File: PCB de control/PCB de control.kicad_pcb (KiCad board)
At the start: 4 copper layers, 68.3 x 60 mm, 83 parts, among them J1 Conn_01x12_Pin, Q1 DMP4015SPSQ-13, U1 ESP32-C6-MINI-1U-H4, U2 DRV8434PWPR, U3 TPS54302DDCT, U4 TPS62162DSG, U5 D3V3XA4B10LP

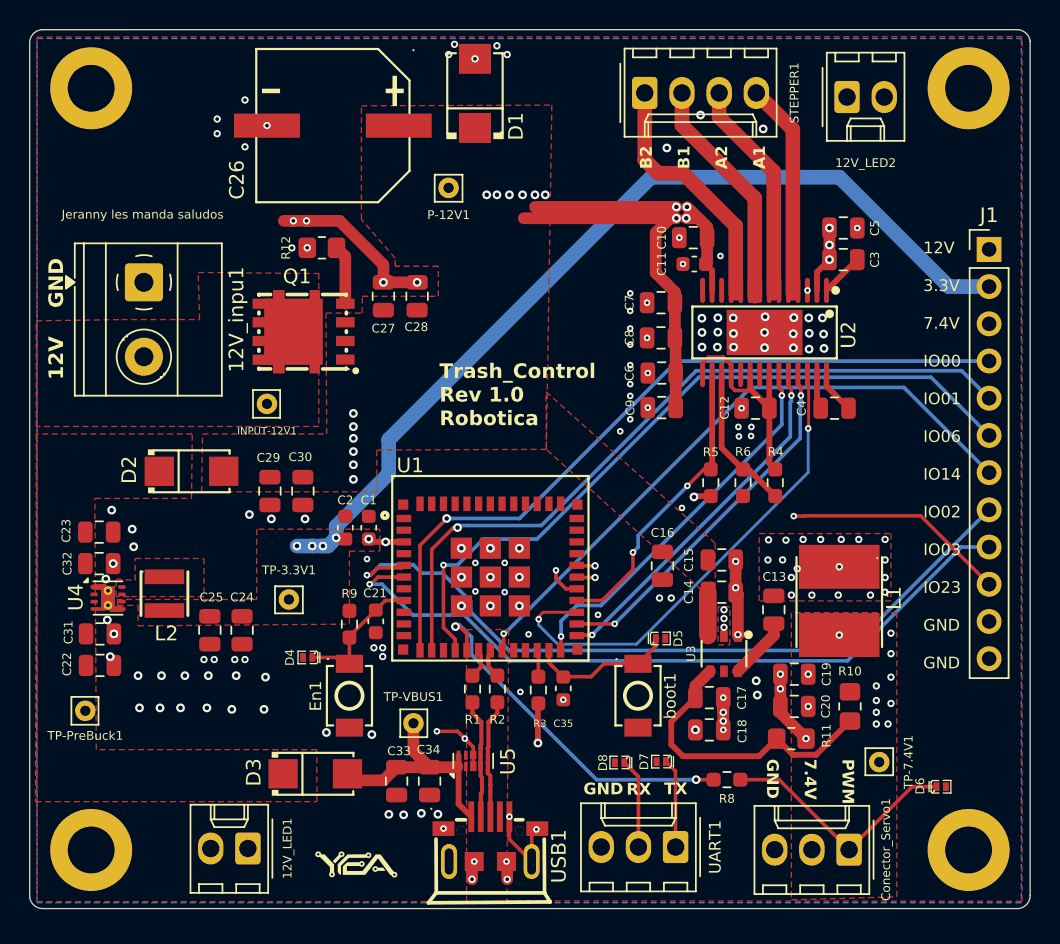
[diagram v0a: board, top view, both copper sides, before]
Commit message: Cambio de vias a mayor tamaño / Para disminutir Costes
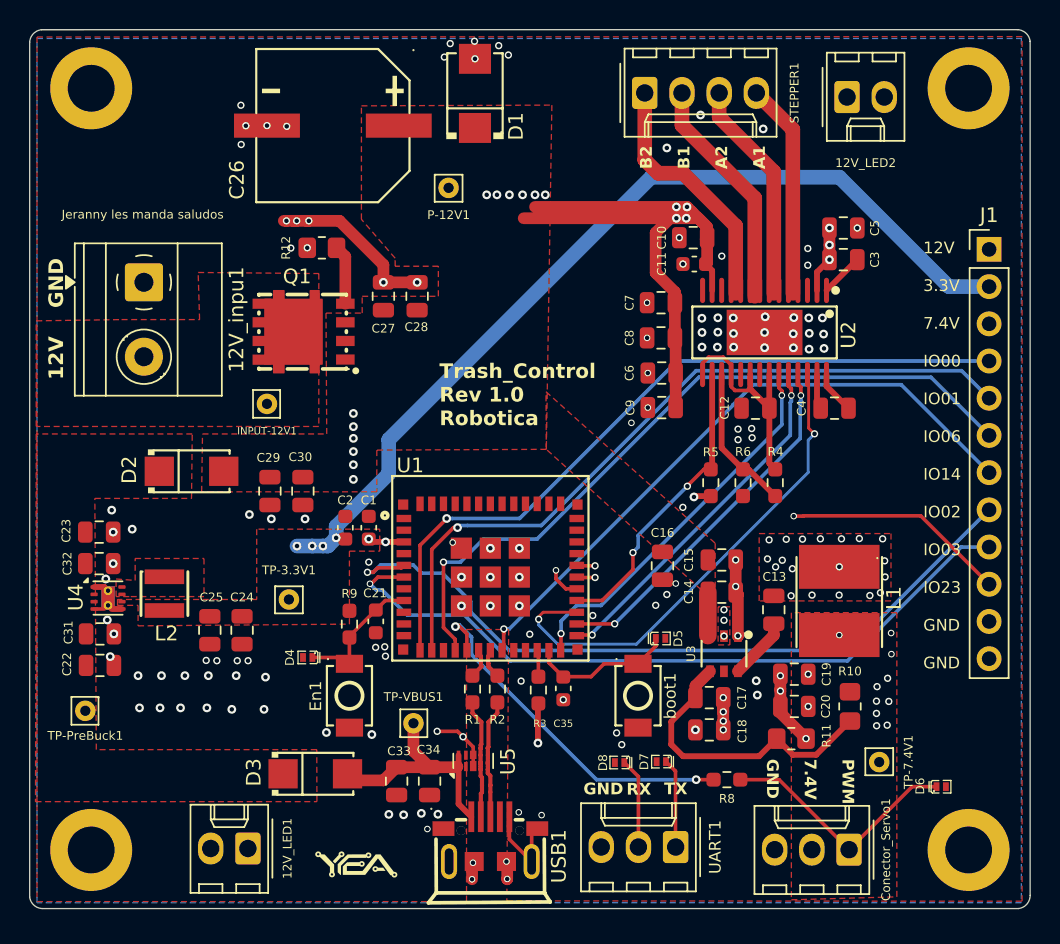
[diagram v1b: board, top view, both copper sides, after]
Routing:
- net GND: track 37.9 -> 37.2 mm, vias 138 -> 131
- net GPIO14: track 43.7 -> 44.4 mm
- net /SW7: track 13.5 -> 14.1 mm
